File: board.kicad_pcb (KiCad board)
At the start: 2 copper layers, 91 x 75 mm, 21 parts, among them J1 Z-AXIS, J10 Conn_01x02_Male, J11 Conn_01x04_Male, J12 CHOOSE, J2 Y-AXIS, J3 Y-AXIS, J4 X-AXIS, J5 12-36V, J6 12V, J7 Conn_02x14_Odd_Even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

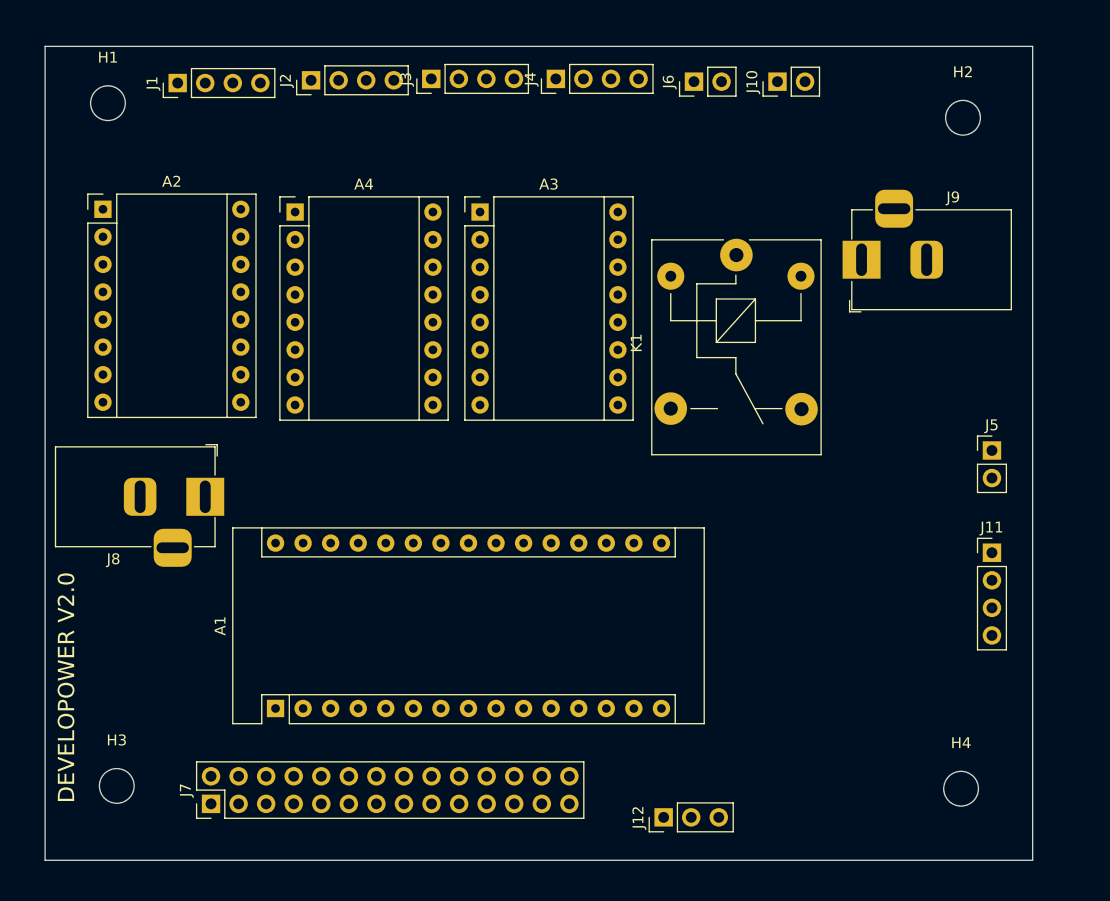
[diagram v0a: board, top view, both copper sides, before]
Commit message: Add more details (extra components, footprints and 3d models)
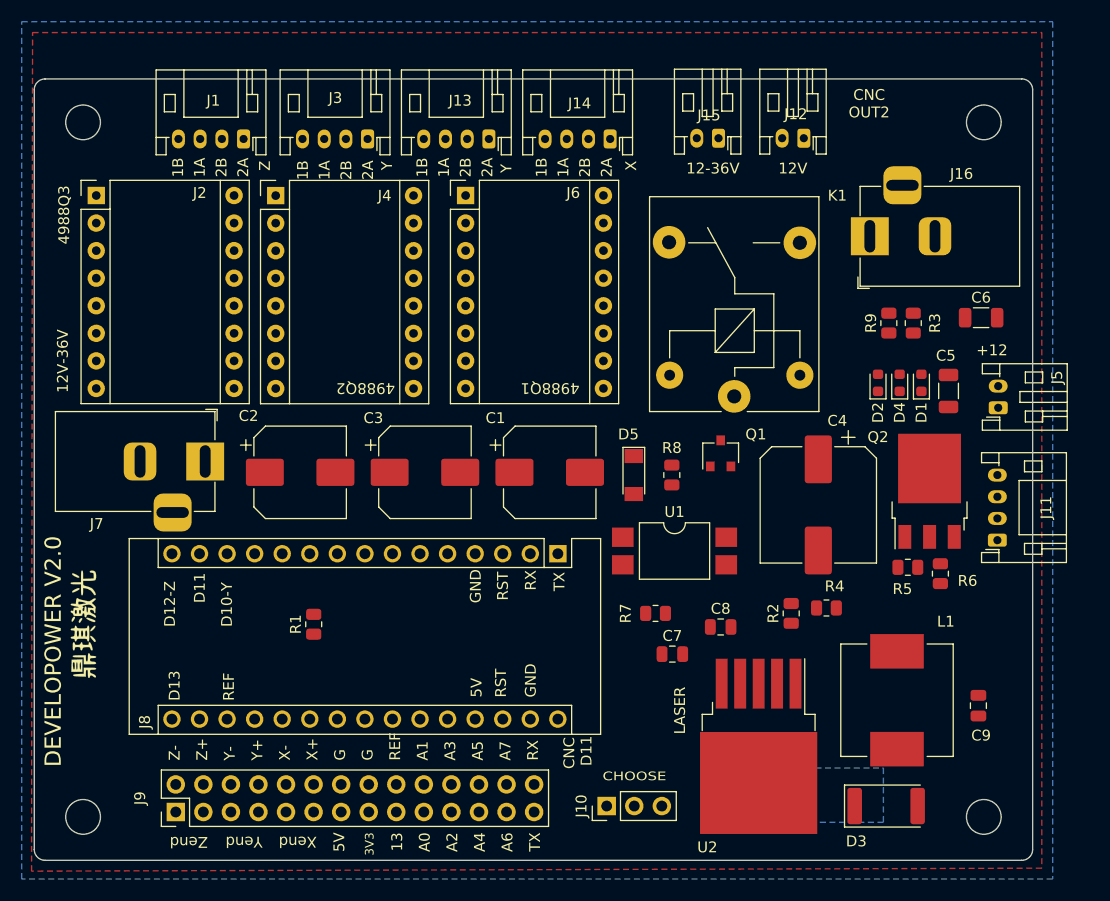
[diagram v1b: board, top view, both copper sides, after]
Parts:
- removed the J10 at (172.6, 63.5)
- removed the J4 at (152.2, 63.3)
- added C1: 220/35V, Capacitor_SMD:CP_Elec_8x10, F.Cu at (151.7, 99.5)
- added C2: 220/35V, Capacitor_SMD:CP_Elec_8x10, F.Cu at (128.7, 99.5)
- added C3: 220/35V, Capacitor_SMD:CP_Elec_8x10, F.Cu at (140.2, 99.5)
- added C4: 220/50V, Capacitor_SMD:CP_Elec_10x10.5, F.Cu at (176.4, 102.5)
- added C5: 100n, Capacitor_SMD:C_1206_3216Metric, F.Cu at (188.4, 92.0)
- added C6: 100n, Capacitor_SMD:C_1206_3216Metric, F.Cu at (191.4, 85.3)
- added C7: 100n, Capacitor_SMD:C_0805_2012Metric, F.Cu at (163.0, 116.3)
- added C8: 100n, Capacitor_SMD:C_0805_2012Metric, F.Cu at (167.4, 113.8)
- added C9: 100n, Capacitor_SMD:C_0805_2012Metric, F.Cu at (191.2, 121.0)
- added D1: LED, LED_SMD:LED_0603_1608Metric, F.Cu at (185.9, 91.3)
- added D2: LED, LED_SMD:LED_0603_1608Metric, F.Cu at (181.9, 91.3)
- added D3: SS54, Diode_SMD:D_2512_6332Metric, F.Cu at (182.7, 130.3)
- added D4: LED, LED_SMD:LED_0603_1608Metric, F.Cu at (183.9, 91.3)
- added D5: LED, Diode_SMD:D_MiniMELF, F.Cu at (159.4, 99.8)
- added J12: Conn_01x02_Male, Connector_JST:JST_PH_S2B-PH-K_1x02_P2.00mm_Horizontal, F.Cu at (175.1, 68.7)
- added J14: X, Connector_JST:JST_PH_S4B-PH-K_1x04_P2.00mm_Horizontal, F.Cu at (157.2, 68.8)
- added L1: 470, Inductor_SMD:L_Vishay_IHLP-4040, F.Cu at (183.7, 120.5)
- added Q1: Y2, Package_TO_SOT_SMD:SC-59, F.Cu at (167.4, 97.8)
- added Q2: WJ0625A, Package_TO_SOT_SMD:TO-252-3_TabPin2, F.Cu at (186.7, 101.3)
- added R1: 10K, Resistor_SMD:R_0805_2012Metric, F.Cu at (129.9, 113.5)
- added R2: 1k8, Resistor_SMD:R_0805_2012Metric, F.Cu at (173.9, 112.5)
- added R3: 2k, Resistor_SMD:R_0805_2012Metric, F.Cu at (185.2, 85.8)
- added R4: 16k, Resistor_SMD:R_0805_2012Metric, F.Cu at (177.2, 112.0)
- added R5: 10k, Resistor_SMD:R_0805_2012Metric, F.Cu at (184.7, 108.3)
- added R6: 100k, Resistor_SMD:R_0805_2012Metric, F.Cu at (187.7, 108.9)
- added R7: 1k, Resistor_SMD:R_0805_2012Metric, F.Cu at (161.4, 112.5)
- added R8: 4k7, Resistor_SMD:R_0805_2012Metric, F.Cu at (162.9, 99.8)
- added R9: 5k, Resistor_SMD:R_0805_2012Metric, F.Cu at (182.9, 85.8)
- added T1: Logo_Open_Hardware_Small, Developower:chinese-text, F.Cu at (108.7, 113.5)
- added U1: PC817, Package_DIP:SMDIP-4_W9.53mm, F.Cu at (163.2, 106.8)
- added U2: XL4015E1, Package_TO_SOT_SMD:TO-263-5_TabPin6, F.Cu at (170.9, 124.8)
- J1: value Z-AXIS -> Z; footprint Connector_PinHeader_2.54mm:PinHeader_1x04_P2.54mm_Vertical -> Connector_JST:JST_PH_S4B-PH-K_1x04_P2.00mm_Horizontal
- J11: footprint Connector_PinHeader_2.54mm:PinHeader_1x04_P2.54mm_Vertical -> Connector_JST:JST_PH_S4B-PH-K_1x04_P2.00mm_Horizontal
- J13: renamed from J3; value Y-AXIS -> Y; footprint Connector_PinHeader_2.54mm:PinHeader_1x04_P2.54mm_Vertical -> Connector_JST:JST_PH_S4B-PH-K_1x04_P2.00mm_Horizontal
- J15: renamed from J6; footprint Connector_PinHeader_2.54mm:PinHeader_1x02_P2.54mm_Vertical -> Connector_JST:JST_PH_S2B-PH-K_1x02_P2.00mm_Horizontal
- J16: renamed from J9; footprint Connector_BarrelJack:BarrelJack_Horizontal -> Developower:BarrelJack_Horizontal
- J2: renamed from A2; footprint Module:Pololu_Breakout-16_15.2x20.3mm -> Developower:Pololu_Breakout-16_15.2x20.3mm
- J3: renamed from J2; value Y-AXIS -> Y; footprint Connector_PinHeader_2.54mm:PinHeader_1x04_P2.54mm_Vertical -> Connector_JST:JST_PH_S4B-PH-K_1x04_P2.00mm_Horizontal
- J4: renamed from A3; footprint Module:Pololu_Breakout-16_15.2x20.3mm -> Developower:Pololu_Breakout-16_15.2x20.3mm
- J5: footprint Connector_PinHeader_2.54mm:PinHeader_1x02_P2.54mm_Vertical -> Connector_JST:JST_PH_S2B-PH-K_1x02_P2.00mm_Horizontal
- J6: renamed from A4; footprint Module:Pololu_Breakout-16_15.2x20.3mm -> Developower:Pololu_Breakout-16_15.2x20.3mm
- J7: renamed from J8; footprint Connector_BarrelJack:BarrelJack_Horizontal -> Developower:BarrelJack_Horizontal
- J8: renamed from A1; footprint Module:Arduino_Nano -> Developower:Arduino_Nano
- moved J8 29.7 mm to (152.4, 107.0), turned to 270 degrees
- moved J4 18.9 mm to (126.4, 74.0)
- moved J6 15.8 mm to (143.9, 74.0)
- moved K1 13.0 mm to (168.7, 92.5), turned to 90 degrees
- moved J1 7.96 mm to (123.4, 68.8), turned to 180 degrees
- moved J13 7.67 mm to (146.1, 68.8), turned to 180 degrees
- moved J3 7.51 mm to (134.9, 68.8), turned to 180 degrees
- moved J15 5.68 mm to (167.2, 68.7), turned to 180 degrees
- moved J10 5.35 mm to (156.9, 130.3)
- moved H3 4.22 mm to (108.7, 131.3)
- moved J5 3.97 mm to (193.0, 93.6), turned to 90 degrees
- moved H4 3.34 mm to (191.7, 131.3)
- moved J9 3.34 mm to (117.2, 130.8)
- moved J7 3.25 mm to (119.9, 98.5)
- moved H1 2.89 mm to (108.7, 67.3)
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- renumbered J12 to J10, J7 to J9
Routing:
- added copper zone on B.Cu, net (none)
- added copper zone on B.Cu, net GND
- added copper zone on F.Cu, net GND
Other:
- board size 91 x 75 mm -> 92 x 72 mm
- board text added: "12-36V"
- board text added: "12V"
- board text added: "12V-36V"
- board text added: "13"
- board text added: "1A"
- board text added: "1B"
- board text added: "2A"
- board text added: "2B"
- board text added: "3V3"
- board text added: "4988Q1"
- board text added: "4988Q2"
- board text added: "4988Q3"
- board text added: "5V"
- board text added: "A0"
- board text added: "A1"
- board text added: "A2"
- board text added: "A3"
- board text added: "A4"
- board text added: "A5"
- board text added: "A6"
- board text added: "A7"
- board text added: "CHOOSE"
- board text added: "CNC"
- board text added: "CNC OUT2"
- board text added: "D10-Y"
- board text added: "D11"
- board text added: "D12-Z"
- board text added: "D13"
- board text added: "G"
- board text added: "GND"
- board text added: "LASER"
- board text added: "REF"
- board text added: "RST"
- board text added: "RX"
- board text added: "TX"
- board text added: "X+"
- board text added: "X-"
- board text added: "Xend"
- board text added: "Y+"
- board text added: "Y-"
- board text added: "Yend"
- board text added: "Z+"
- board text added: "Z-"
- board text added: "Zend"

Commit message: Add some interconnections. Fix some missing 3d models.
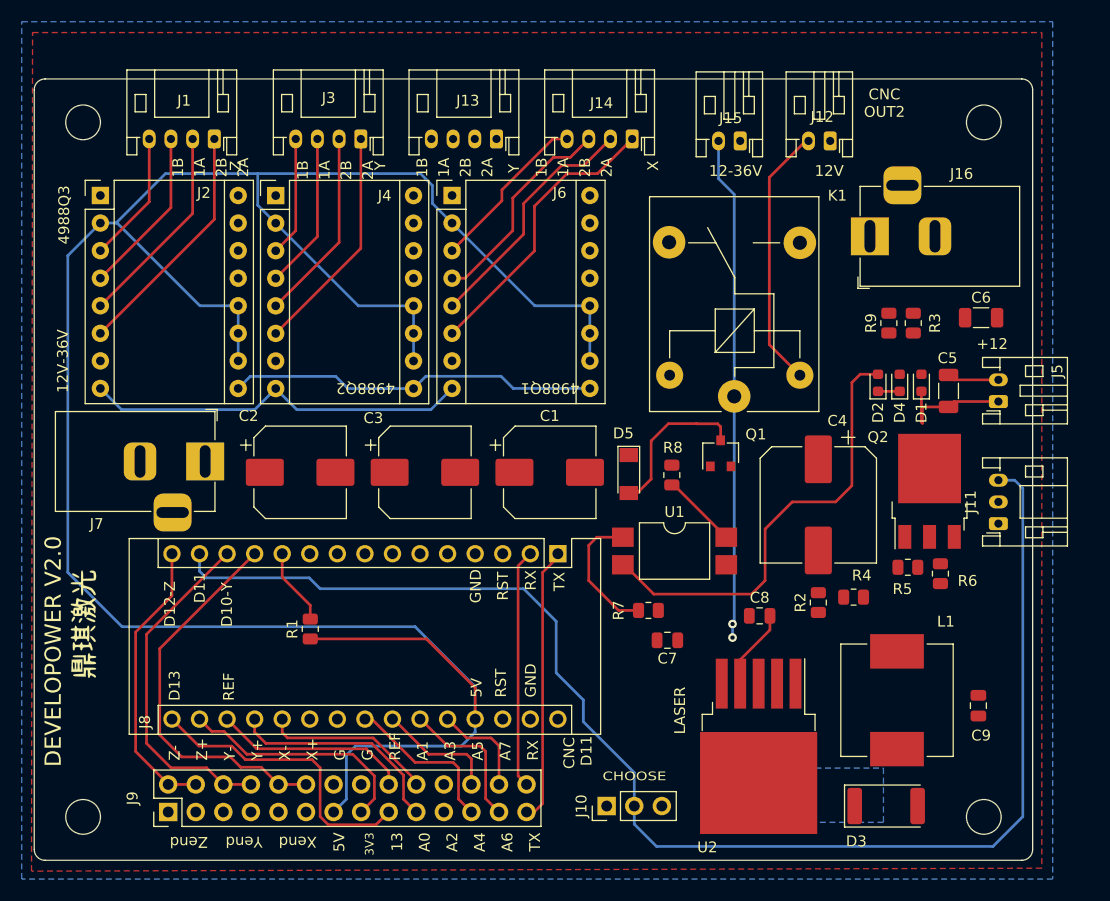
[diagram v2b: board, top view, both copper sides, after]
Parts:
- J10: value CHOOSE -> CNC/Laser
- J11: value Conn_01x04_Male -> Conn_01x03_Male; footprint Connector_JST:JST_PH_S4B-PH-K_1x04_P2.00mm_Horizontal -> Connector_JST:JST_PH_S3B-PH-K_1x03_P2.00mm_Horizontal
- J12: value Conn_01x02_Male -> 12V
- J15: value 12V -> 12V-36V
- J8: value Arduino_Nano_v3.x -> Arduino_Nano
- J9: value Conn_02x14_Odd_Even -> Misc
- moved C8 3.74 mm to (171.0, 112.8)
- moved J1 2.69 mm to (120.8, 68.8)
- moved R2 2.69 mm to (176.4, 111.5)
- moved R4 2.69 mm to (179.7, 111.0)
- moved J12 2.44 mm to (177.5, 69.0)
- moved J14 2.02 mm to (159.2, 68.8)
- moved J15 2.02 mm to (169.2, 69.0)
- moved J11 1.53 mm to (193.0, 104.2)
- moved C7 1.35 mm to (162.5, 115.0), turned to 180 degrees
- moved J6 1.25 mm to (142.7, 74.0)
- moved R7 0.71 mm to (160.8, 112.2), turned to 180 degrees
- moved J13 0.70 mm to (146.8, 68.8)
- moved J9 0.70 mm to (116.5, 130.8)
- moved J3 0.62 mm to (134.2, 68.8)
- moved J5 0.58 mm to (193.0, 93.0)
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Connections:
- C1 pad 2: (no net) -> GND
- C2 pad 2: (no net) -> GND
- C3 pad 2: (no net) -> GND
- C4 pad 2: (no net) -> GND
- C5 pad 1: (no net) -> GND
- C5 pad 2: (no net) -> Net-(C5-Pad2)
- C6 pad 2: (no net) -> GND
- C7 pad 1: (no net) -> Net-(C7-Pad1)
- C7 pad 2: (no net) -> GND
- C8 pad 1: (no net) -> GND
- C8 pad 2: (no net) -> Net-(C7-Pad1)
- C9 pad 2: (no net) -> GND
- D1 pad 1: (no net) -> GND
- D1 pad 2: (no net) -> Net-(D1-Pad2)
- D2 pad 1: (no net) -> GND
- D2 pad 2: (no net) -> Net-(D2-Pad2)
- D3 pad 2: (no net) -> Net-(D3-Pad2)
- D4 pad 1: (no net) -> GND
- D4 pad 2: (no net) -> Net-(D4-Pad2)
- D5 pad 2: (no net) -> Net-(D5-Pad2)
- J1 pad 1: (no net) -> /Z.2B
- J1 pad 2: (no net) -> /Z.2A
- J1 pad 3: (no net) -> /Z.1A
- J1 pad 4: (no net) -> /Z.1B
- J10 pad 2: (no net) -> /D11
- J11 pad 2: (no net) -> GND
- J11 pad 3: (no net) -> /D11
- J12 pad 1: (no net) -> GND
- J12 pad 2: (no net) -> /relay.p2
- J14 pad 1: (no net) -> /X.2B
- J14 pad 2: (no net) -> /X.2A
- J14 pad 3: (no net) -> /X.1A
- J14 pad 4: (no net) -> /X.1B
- J15 pad 1: (no net) -> GND
- J15 pad 2: (no net) -> /relay.common
- J16 pad 2: (no net) -> GND
- J16 pad 3: (no net) -> GND
- J2 pad 1: (no net) -> GND
- J2 pad 10: (no net) -> +5V
- J2 pad 11: (no net) -> +5V
- J2 pad 12: (no net) -> +5V
- J2 pad 2: (no net) -> +5V
- J2 pad 3: (no net) -> /Z.1B
- J2 pad 4: (no net) -> /Z.1A
- J2 pad 5: (no net) -> /Z.2A
- J2 pad 6: (no net) -> /Z.2B
- J2 pad 7: (no net) -> GND
- J2 pad 8: (no net) -> /VMOT
- J2 pad 9: (no net) -> /EN
- J3 pad 1: (no net) -> /Y.2B
- J3 pad 2: (no net) -> /Y.2A
- J3 pad 3: (no net) -> /Y.1A
- J3 pad 4: (no net) -> /Y.1B
- J4 pad 1: (no net) -> GND
- J4 pad 10: (no net) -> +5V
- J4 pad 11: (no net) -> +5V
- J4 pad 12: (no net) -> +5V
- J4 pad 2: (no net) -> +5V
- J4 pad 3: (no net) -> /Y.1B
- J4 pad 4: (no net) -> /Y.1A
- J4 pad 5: (no net) -> /Y.2A
- J4 pad 6: (no net) -> /Y.2B
- J4 pad 7: (no net) -> GND
- J4 pad 8: (no net) -> /VMOT
- J4 pad 9: (no net) -> /EN
- J5 pad 1: (no net) -> GND
- J5 pad 2: (no net) -> Net-(C5-Pad2)
- J6 pad 1: (no net) -> GND
- J6 pad 10: (no net) -> +5V
- J6 pad 11: (no net) -> +5V
- J6 pad 12: (no net) -> +5V
- J6 pad 2: (no net) -> +5V
- J6 pad 3: (no net) -> /X.1B
- J6 pad 4: (no net) -> /X.1A
- J6 pad 5: (no net) -> /X.2A
- J6 pad 6: (no net) -> /X.2B
- J6 pad 7: (no net) -> GND
- J6 pad 8: (no net) -> /VMOT
- J6 pad 9: (no net) -> /EN
- J7 pad 2: (no net) -> GND
- J7 pad 3: (no net) -> GND
- J8 pad 1: (no net) -> /TX
- J8 pad 11: (no net) -> /D8
- J8 pad 12: (no net) -> /D9
- J8 pad 13: (no net) -> /D10
- J8 pad 14: (no net) -> /D11
- J8 pad 15: (no net) -> /D12
- J8 pad 16: (no net) -> /D13
- J8 pad 18: (no net) -> /REF
- J8 pad 19: (no net) -> /A0
- J8 pad 2: (no net) -> /RX
- J8 pad 20: (no net) -> /A1
- J8 pad 21: (no net) -> /A2
- J8 pad 22: (no net) -> /A3
- J8 pad 23: (no net) -> /A4
- J8 pad 24: (no net) -> /A5
- J8 pad 25: (no net) -> /A6
- J8 pad 26: (no net) -> /A7
- J9 pad 1: (no net) -> GND
- J9 pad 10: (no net) -> /D9
- J9 pad 11: (no net) -> GND
- J9 pad 12: (no net) -> /D9
- J9 pad 14: /G -> GND
- J9 pad 16: /G -> GND
- J9 pad 17: (no net) -> /D13
- J9 pad 18: (no net) -> /REF
- J9 pad 19: (no net) -> /A0
- J9 pad 2: (no net) -> /D12
- J9 pad 20: (no net) -> /A1
- J9 pad 21: (no net) -> /A2
- J9 pad 22: (no net) -> /A3
- J9 pad 23: (no net) -> /A4
- J9 pad 24: (no net) -> /A5
- J9 pad 25: (no net) -> /A6
- J9 pad 26: (no net) -> /A7
- J9 pad 27: (no net) -> /TX
- J9 pad 28: (no net) -> /RX
- J9 pad 3: (no net) -> GND
- J9 pad 4: (no net) -> /D12
- J9 pad 5: (no net) -> GND
- J9 pad 6: (no net) -> /D10
- J9 pad 7: (no net) -> GND
- J9 pad 8: (no net) -> /D10
- J9 pad 9: (no net) -> GND
- K1 pad 1: (no net) -> /relay.common
- K1 pad 2: (no net) -> /relay.p2
- Q1 pad 2: (no net) -> GND
- Q1 pad 3: (no net) -> Net-(D5-Pad2)
- R1 pad 1: (no net) -> +5V
- R1 pad 2: (no net) -> /D8
- R3 pad 1: (no net) -> Net-(C5-Pad2)
- R3 pad 2: (no net) -> Net-(D1-Pad2)
- R7 pad 2: (no net) -> Net-(R7-Pad2)
- R8 pad 2: (no net) -> Net-(R8-Pad2)
- R9 pad 1: (no net) -> Net-(C5-Pad2)
- R9 pad 2: (no net) -> Net-(D4-Pad2)
- U1 pad 1: (no net) -> Net-(R7-Pad2)
- U1 pad 2: (no net) -> Net-(D2-Pad2)
- U1 pad 3: (no net) -> GND
- U1 pad 4: (no net) -> Net-(R8-Pad2)
- U2 pad 4: (no net) -> Net-(C7-Pad1)
- U2 pad 6: (no net) -> Net-(D3-Pad2)
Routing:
- net +5V: track 0.00 -> 222.0 mm
- net /D11: track 0.00 -> 128.7 mm
- net /relay.common: track 0.00 -> 46.7 mm, vias 0 -> 2
- net Net-(D2-Pad2): track 0.00 -> 41.4 mm
- net /D9: track 0.00 -> 35.7 mm
- net /VMOT: track 0.00 -> 35.6 mm
- net /EN: track 0.00 -> 34.3 mm
- net /D10: track 0.00 -> 31.7 mm
- net /D13: track 0.00 -> 27.1 mm
- net /D12: track 0.00 -> 26.4 mm
- net /X.2B: track 0.00 -> 26.4 mm
- net /TX: track 0.00 -> 24.7 mm
- net /relay.p2: track 0.00 -> 24.5 mm
- net /X.2A: track 0.00 -> 22.6 mm
- net /Z.2B: track 0.00 -> 22.3 mm
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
